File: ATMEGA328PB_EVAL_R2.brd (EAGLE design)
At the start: 40.6 x 41.9 mm, 14 parts, among them U2 ATMEGA328PB-AU

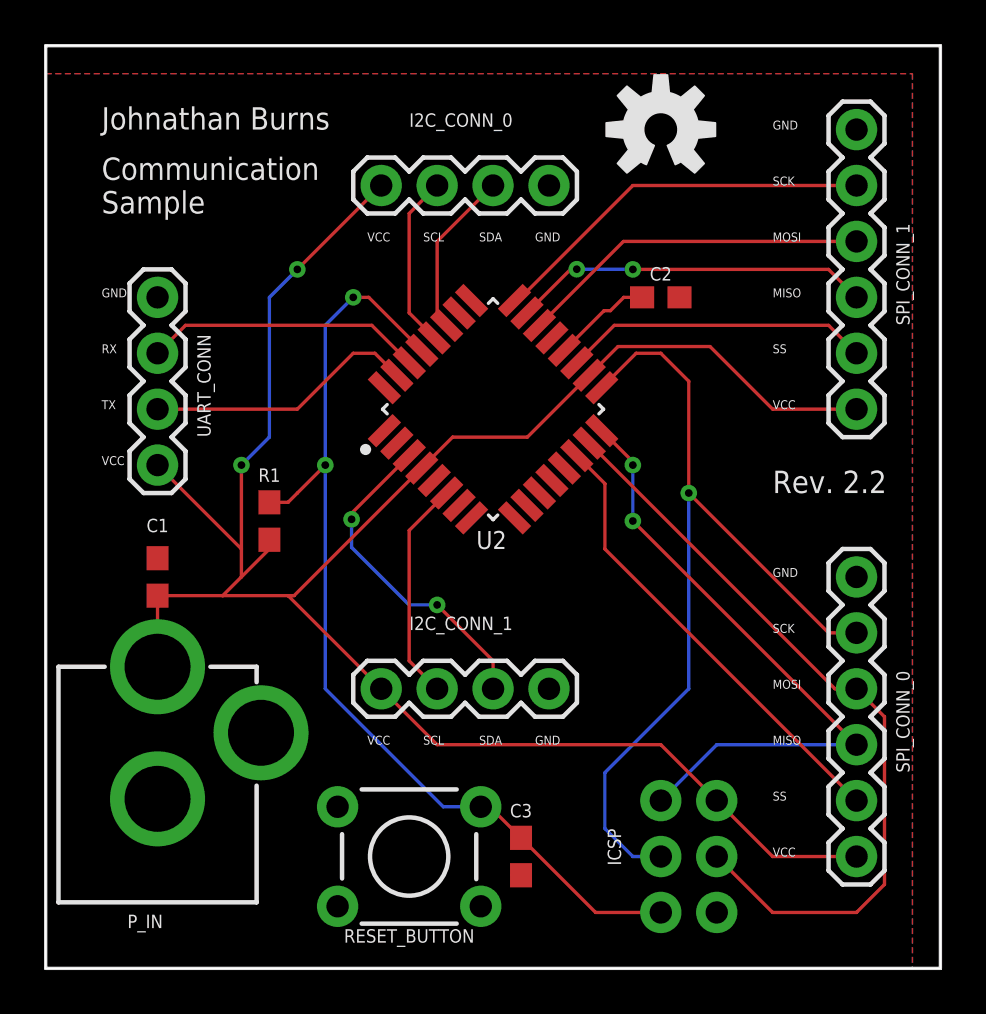
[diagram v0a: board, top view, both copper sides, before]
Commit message: Enlarged main power trace(s)
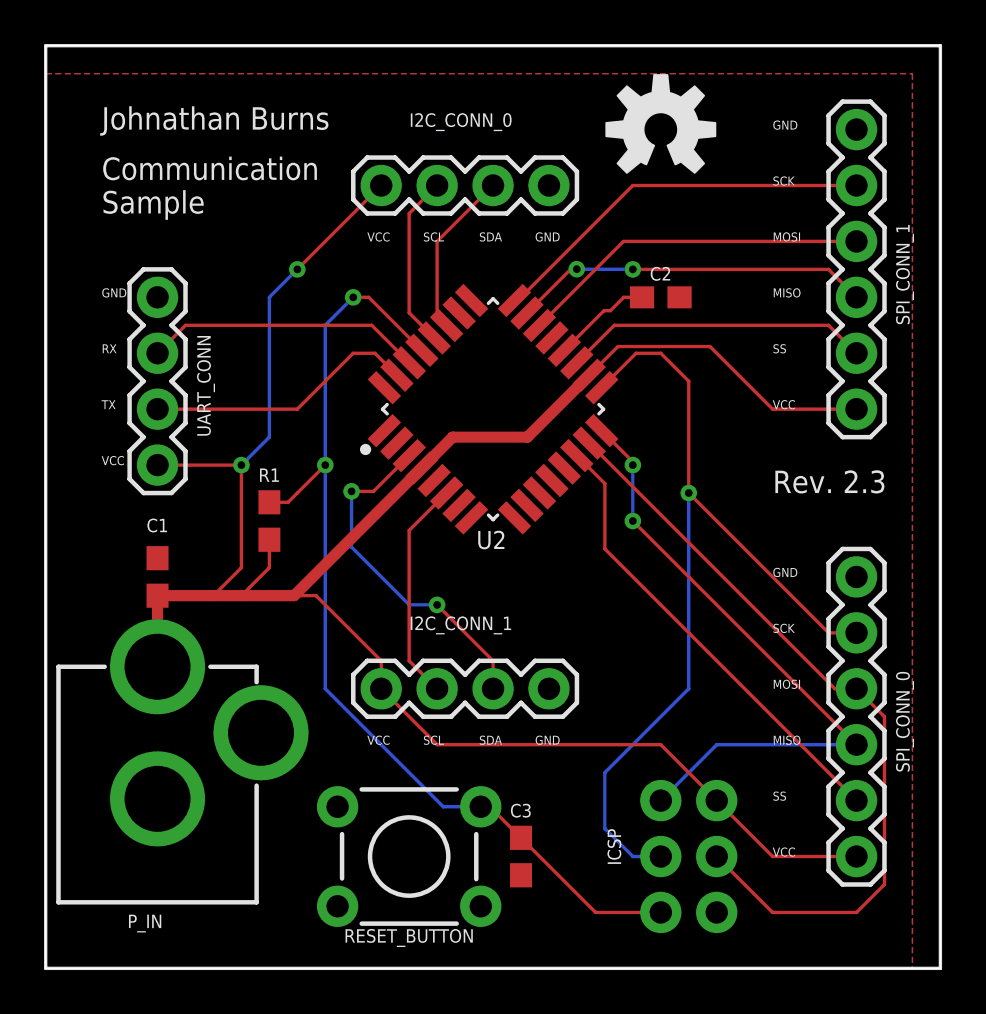
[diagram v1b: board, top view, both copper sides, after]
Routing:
- net SDA1: track 15.1 -> 15.7 mm
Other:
- board text added: "Rev. 2.3"
- board text removed: "Rev. 2.2"
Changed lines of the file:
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@@
 <text x="2.54" y="34.29" size="1.016" layer="21">Communication
 Sample</text>
-<text x="33.02" y="21.59" size="1.016" layer="21">Rev. 2.2</text>
+<text x="33.02" y="21.59" size="1.016" layer="21">Rev. 2.3</text>
 <wire x1="0" y1="0" x2="0" y2="41.91" width="0.1524" layer="25"/>
 <wire x1="0" y1="41.91" x2="40.64" y2="41.91" width="0.1524" layer="25"/>
@@
 <contactref element="I2C_CONN_1" pad="1"/>
 <contactref element="ICSP" pad="2"/>
-<wire x1="5.08" y1="16.93" x2="5.08" y2="13.7" width="0.1524" layer="1"/>
+<wire x1="5.08" y1="16.93" x2="5.08" y2="13.7" width="0.508" layer="1"/>
 <wire x1="36.83" y1="5.08" x2="33.02" y2="5.08" width="0.1524" layer="1"/>
 <wire x1="33.02" y1="5.08" x2="30.48" y2="7.62" width="0.1524" layer="1"/>
-<wire x1="5.08" y1="16.93" x2="8.04" y2="16.93" width="0.1524" layer="1"/>
-<wire x1="11.01" y1="16.93" x2="11.284315625" y2="16.93" width="0.1524" layer="1"/>
-<wire x1="11.284315625" y1="16.93" x2="17.08145" y2="22.727134375" width="0.1524" layer="1"/>
-<wire x1="5.08" y1="22.86" x2="8.89" y2="19.05" width="0.1524" layer="1"/>
-<wire x1="8.89" y1="19.05" x2="8.89" y2="17.78" width="0.1524" layer="1"/>
-<wire x1="8.04" y1="16.93" x2="8.89" y2="17.78" width="0.1524" layer="1"/>
-<wire x1="15.24" y1="12.7" x2="11.01" y2="16.93" width="0.1524" layer="1"/>
-<wire x1="11.01" y1="16.93" x2="8.04" y2="16.93" width="0.1524" layer="1"/>
-<wire x1="18.484315625" y1="24.13" x2="17.08145" y2="22.727134375" width="0.1524" layer="1"/>
-<wire x1="24.68991875" y1="26.941490625" x2="21.878428125" y2="24.13" width="0.1524" layer="1"/>
-<wire x1="21.878428125" y1="24.13" x2="18.484315625" y2="24.13" width="0.1524" layer="1"/>
+<wire x1="5.08" y1="16.93" x2="7.62" y2="16.93" width="0.508" layer="1"/>
+<wire x1="7.62" y1="16.93" x2="8.89" y2="16.93" width="0.508" layer="1"/>
+<wire x1="18.484315625" y1="24.13" x2="17.08145" y2="22.727134375" width="0.508" layer="1"/>
+<wire x1="24.68991875" y1="26.941490625" x2="21.878428125" y2="24.13" width="0.508" layer="1"/>
+<wire x1="21.878428125" y1="24.13" x2="18.484315625" y2="24.13" width="0.508" layer="1"/>
 <wire x1="24.68991875" y1="26.941490625" x2="25.993228125" y2="28.2448" width="0.1524" layer="1"/>
 <wire x1="30.1752" y1="28.2448" x2="33.02" y2="25.4" width="0.1524" layer="1"/>
@@
 <wire x1="10.16" y1="24.13" x2="8.89" y2="22.86" width="0.1524" layer="16"/>
 <via x="8.89" y="22.86" extent="1-16" drill="0.35"/>
-<wire x1="8.89" y1="22.86" x2="8.89" y2="19.05" width="0.1524" layer="1"/>
 <wire x1="15.24" y1="12.7" x2="17.78" y2="10.16" width="0.1524" layer="1"/>
-<wire x1="8.89" y1="17.78" x2="10.16" y2="19.05" width="0.1524" layer="1"/>
-<wire x1="10.16" y1="19.05" x2="10.16" y2="19.47" width="0.1524" layer="1"/>
 <wire x1="17.78" y1="10.16" x2="27.94" y2="10.16" width="0.1524" layer="1"/>
 <wire x1="27.94" y1="10.16" x2="30.48" y2="7.62" width="0.1524" layer="1"/>
+<wire x1="8.89" y1="16.93" x2="11.284315625" y2="16.93" width="0.508" layer="1"/>
+<wire x1="11.284315625" y1="16.93" x2="17.08145" y2="22.727134375" width="0.508" layer="1"/>
+<wire x1="10.16" y1="19.47" x2="10.16" y2="18.2" width="0.1524" layer="1"/>
+<wire x1="10.16" y1="18.2" x2="8.89" y2="16.93" width="0.1524" layer="1"/>
+<wire x1="5.08" y1="22.86" x2="8.89" y2="22.86" width="0.1524" layer="1"/>
+<wire x1="8.89" y1="22.86" x2="8.89" y2="18.2" width="0.1524" layer="1"/>
+<wire x1="8.89" y1="18.2" x2="7.62" y2="16.93" width="0.1524" layer="1"/>
+<wire x1="15.24" y1="12.7" x2="15.24" y2="13.97" width="0.1524" layer="1"/>
+<wire x1="15.24" y1="13.97" x2="12.28" y2="16.93" width="0.1524" layer="1"/>
+<wire x1="12.28" y1="16.93" x2="11.284315625" y2="16.93" width="0.1524" layer="1"/>
 </signal>
 <signal name="SCK0">
@@
 <contactref element="U2" pad="3"/>
 <contactref element="I2C_CONN_1" pad="3"/>
-<wire x1="16.5157625" y1="23.29281875" x2="13.893084375" y2="20.670140625" width="0.1524" layer="1"/>
-<wire x1="13.893084375" y1="20.670140625" x2="13.893084375" y2="20.396915625" width="0.1524" layer="1"/>
-<via x="13.893084375" y="20.396915625" extent="1-16" drill="0.35"/>
-<wire x1="13.893084375" y1="20.396915625" x2="13.893084375" y2="19.126915625" width="0.1524" layer="16"/>
+<wire x1="16.5157625" y1="23.29281875" x2="14.889859375" y2="21.666915625" width="0.1524" layer="1"/>
+<wire x1="14.889859375" y1="21.666915625" x2="13.893084375" y2="21.666915625" width="0.1524" layer="1"/>
+<via x="13.893084375" y="21.666915625" extent="1-16" drill="0.35"/>
+<wire x1="13.893084375" y1="21.666915625" x2="13.893084375" y2="19.126915625" width="0.1524" layer="16"/>
 <wire x1="16.51" y1="16.51" x2="17.78" y2="16.51" width="0.1524" layer="16"/>
 <via x="17.78" y="16.51" extent="1-16" drill="0.35"/>
